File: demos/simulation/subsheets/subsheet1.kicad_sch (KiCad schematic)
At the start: 3 parts

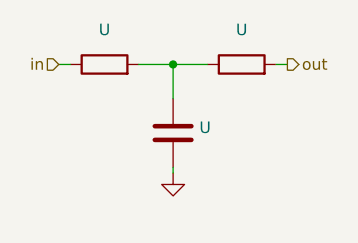
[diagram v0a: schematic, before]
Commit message: feat: update kicad to 9.0.0+dfsg-1
Signed-off-by: lhdjply <lhdjply@126.com>
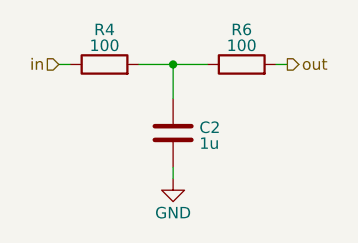
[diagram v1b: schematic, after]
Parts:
- C2: renamed from U; value (none) -> 1u
- R4, R6: renamed from U; value (none) -> 100
